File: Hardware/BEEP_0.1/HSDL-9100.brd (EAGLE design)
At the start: 21.6 x 23.6 mm, 6 parts, among them IC1 HSDL-9100

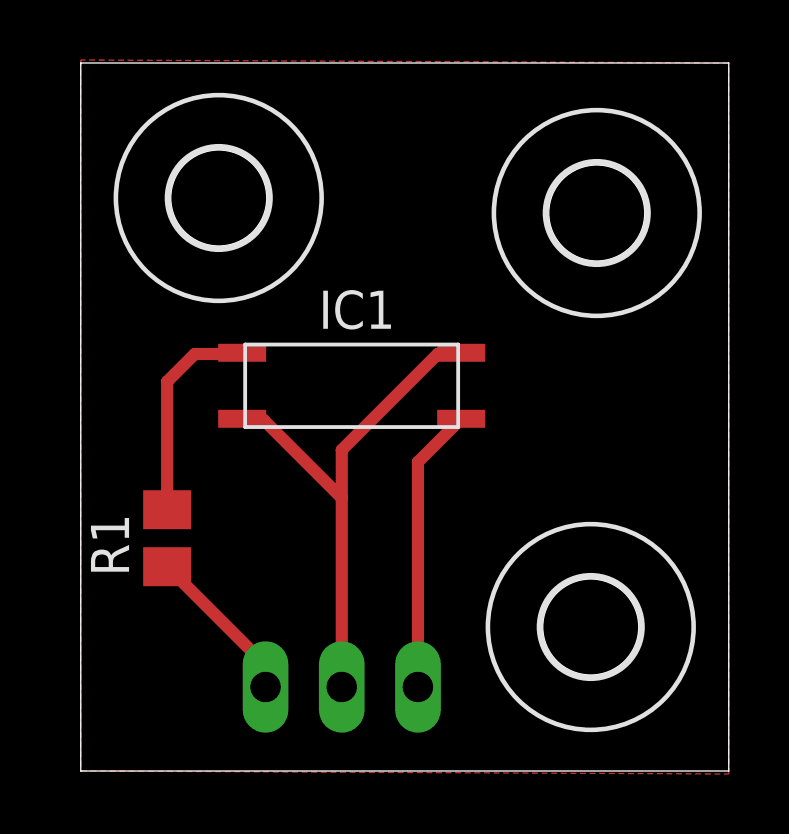
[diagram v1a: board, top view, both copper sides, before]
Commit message: Add branding ;) enhance PCBs finish Easy RGB Board add Texas Instruments libray from Element 14 add dxf import ulp for eagle add Script for easy eagle export to pdf for etching minor cleanup
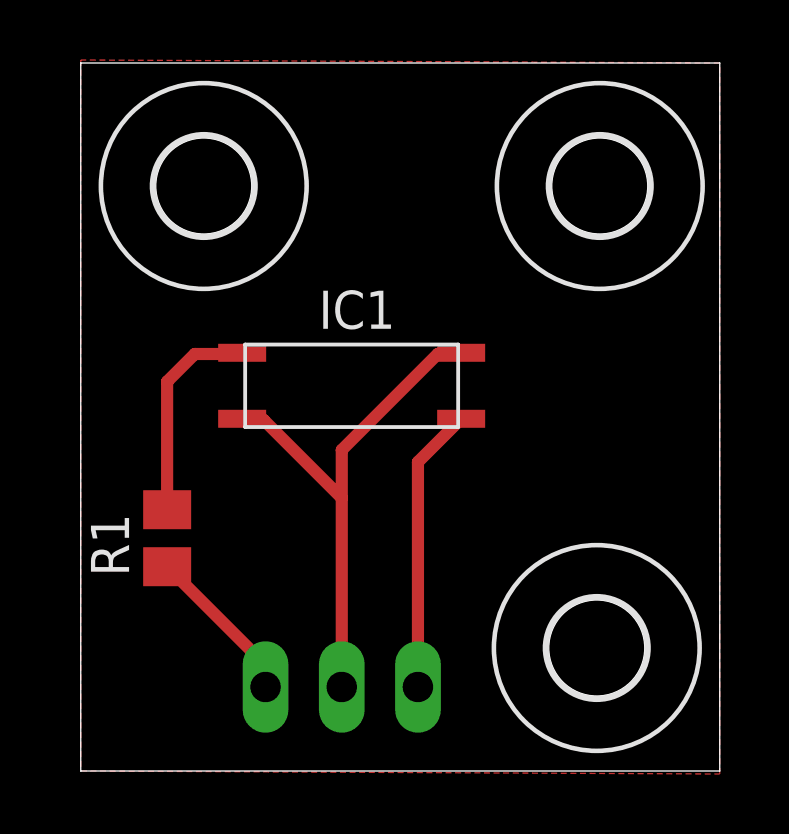
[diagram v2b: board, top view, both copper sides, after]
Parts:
- added U$1: LOGO-COPPER3, Branding:COPPER3
- moved U$4 0.91 mm to (17.3, 19.5)
- moved U$2 0.73 mm to (17.2, 4.10)
- moved U$3 0.64 mm to (4.10, 19.5)
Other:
- board size 21.6 x 23.6 mm -> 21.3 x 23.6 mm
- board text added: "HSDL-9100 v0.1.1"
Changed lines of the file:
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@@
 <layer number="43" name="vRestrict" color="2" fill="10" visible="yes" active="yes"/>
 <layer number="44" name="Drills" color="7" fill="1" visible="no" active="yes"/>
-<layer number="45" name="Holes" color="7" fill="1" visible="no" active="yes"/>
+<layer number="45" name="Holes" color="7" fill="1" visible="yes" active="yes"/>
 <layer number="46" name="Milling" color="3" fill="1" visible="no" active="yes"/>
 <layer number="47" name="Measures" color="7" fill="1" visible="no" active="yes"/>
-<layer number="48" name="Document" color="7" fill="1" visible="yes" active="yes"/>
-<layer number="49" name="Reference" color="7" fill="1" visible="yes" active="yes"/>
+<layer number="48" name="Document" color="7" fill="1" visible="no" active="yes"/>
+<layer number="49" name="Reference" color="7" fill="1" visible="no" active="yes"/>
 <layer number="51" name="tDocu" color="7" fill="1" visible="yes" active="yes"/>
 <layer number="52" name="bDocu" color="7" fill="1" visible="yes" active="yes"/>
@@
 <layer number="97" name="Info" color="7" fill="1" visible="no" active="no"/>
 <layer number="98" name="Guide" color="6" fill="1" visible="no" active="no"/>
+<layer number="100" name="tCName" color="7" fill="1" visible="yes" active="yes"/>
+<layer number="101" name="bCName" color="7" fill="1" visible="yes" active="yes"/>
 </layers>
 <board>
 <plain>
-<wire x1="0" y1="0" x2="21.6" y2="0" width="0" layer="20"/>
-<wire x1="21.6" y1="0" x2="21.6" y2="23.6" width="0" layer="20"/>
-<wire x1="21.6" y1="23.6" x2="0" y2="23.6" width="0" layer="20"/>
+<wire x1="0" y1="0" x2="21.3" y2="0" width="0" layer="20"/>
+<wire x1="21.3" y1="0" x2="21.3" y2="23.6" width="0" layer="20"/>
+<wire x1="21.3" y1="23.6" x2="0" y2="23.6" width="0" layer="20"/>
 <wire x1="0" y1="23.6" x2="0" y2="0" width="0" layer="20"/>
 <text x="7.9" y="4.6" size="1.4224" layer="26" rot="MR90">GND</text>
 <text x="5.3" y="4.7" size="1.4224" layer="26" rot="MR90">LED</text>
 <text x="10.4" y="4.6" size="1.4224" layer="26" rot="MR90">PD</text>
+<text x="15.1" y="9.4" size="0.8128" layer="100">HSDL-9100
+v0.1.1</text>
+<polygon width="0.4064" layer="41">
+<vertex x="21.3" y="15.4"/>
+<vertex x="14.9" y="15.4"/>
+<vertex x="14.9" y="7.5"/>
+<vertex x="21.3" y="7.5"/>
+</polygon>
 </plain>
 <attributes>
@@
 <attribute name="VALUE" x="4.89" y="5.975" size="1.27" layer="28" rot="MR180"/>
 </element>
-<element name="U$2" library="holes" package="3,2" value="" x="17" y="4.8"/>
-<element name="U$3" library="holes" package="3,2" value="" x="4.6" y="19.1"/>
-<element name="U$4" library="holes" package="3,2" value="" x="17.2" y="18.6"/>
+<element name="U$2" library="holes" package="3,2" value="" x="17.2" y="4.1"/>
+<element name="U$3" library="holes" package="3,2" value="" x="4.1" y="19.5"/>
+<element name="U$4" library="holes" package="3,2" value="" x="17.3" y="19.5"/>
+<element name="U$1" library="Branding" package="COPPER3" value="LOGO-COPPER3" x="15.1" y="12.6"/>
 </elements>
 <signals>
@@
 <signal name="GND">
 <polygon width="0.4064" layer="1">
-<vertex x="21.6" y="23.6"/>
+<vertex x="21.3" y="23.6"/>
 <vertex x="0" y="23.7"/>
 <vertex x="0" y="0"/>
-<vertex x="21.6" y="-0.1"/>
+<vertex x="21.3" y="-0.1"/>
 </polygon>
 <contactref element="IC1" pad="LED_K"/>
@@
 </board>
 </drawing>
+<compatibility>
+<note version="6.3" minversion="6.2.2" severity="warning">
+Since Version 6.2.2 text objects can contain more than one line,
+which will not be processed correctly with this version.
+</note>
+</compatibility>
 </eagle>

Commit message: update HSDL-9100 footprint and pcb
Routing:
- net N$4: track 9.62 -> 10.6 mm
- net GND: track 17.6 -> 17.0 mm
- net N$3: track 7.17 -> 6.65 mm
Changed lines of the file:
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@@
 <vertex x="21.3" y="7.5"/>
 </polygon>
+<wire x1="13.7" y1="11.7" x2="11.6" y2="11.7" width="0.4064" layer="41"/>
+<wire x1="11.6" y1="11.7" x2="11.6" y2="12.5" width="0.4064" layer="41"/>
+<wire x1="11.6" y1="12.5" x2="13.7" y2="12.5" width="0.4064" layer="41"/>
+<wire x1="13.7" y1="12.5" x2="13.7" y2="11.7" width="0.4064" layer="41"/>
+<wire x1="4.4" y1="13.1" x2="6.4" y2="13.1" width="0.4064" layer="41"/>
+<wire x1="6.4" y1="13.1" x2="6.4" y2="13.9" width="0.4064" layer="41"/>
+<wire x1="6.4" y1="13.9" x2="4.4" y2="13.9" width="0.4064" layer="41"/>
+<wire x1="4.4" y1="13.9" x2="4.4" y2="13.1" width="0.4064" layer="41"/>
 </plain>
 <attributes>
@@
 <contactref element="IC1" pad="LED_A"/>
 <contactref element="R1" pad="2"/>
-<wire x1="2.88" y1="8.71" x2="2.88" y2="12.98" width="0.4064" layer="1"/>
-<wire x1="2.88" y1="12.98" x2="3.8" y2="13.9" width="0.4064" layer="1"/>
-<wire x1="3.8" y1="13.9" x2="5.34" y2="13.9" width="0.4064" layer="1"/>
-<wire x1="5.34" y1="13.9" x2="5.38" y2="13.94" width="0.4064" layer="1"/>
+<wire x1="2.88" y1="8.71" x2="2.88" y2="12.48" width="0.4064" layer="1"/>
+<wire x1="2.88" y1="12.48" x2="3.8" y2="13.4" width="0.4064" layer="1"/>
+<wire x1="3.8" y1="13.4" x2="5.34" y2="13.4" width="0.4064" layer="1"/>
+<wire x1="5.34" y1="13.4" x2="5.38" y2="13.39" width="0.4064" layer="1"/>
 </signal>
 <signal name="N$4">
 <contactref element="IC1" pad="DET_A"/>
-<wire x1="12.62" y1="11.8" x2="12.68" y2="11.74" width="0.4064" layer="1"/>
-<wire x1="11.24" y1="10.3" x2="12.68" y2="11.74" width="0.4064" layer="1"/>
 <contactref element="JP1" pad="3"/>
-<wire x1="11.24" y1="2.8" x2="11.24" y2="10.3" width="0.4064" layer="1"/>
+<wire x1="11.24" y1="2.8" x2="11.24" y2="11.74" width="0.4064" layer="1"/>
+<wire x1="11.24" y1="11.74" x2="11.8" y2="12.3" width="0.4064" layer="1"/>
+<wire x1="11.8" y1="12.3" x2="12.67" y2="12.3" width="0.4064" layer="1"/>
+<wire x1="12.67" y1="12.3" x2="12.68" y2="12.29" width="0.4064" layer="1"/>
 </signal>
 <signal name="GND">
@@
 </polygon>
 <contactref element="IC1" pad="LED_K"/>
-<wire x1="6.1" y1="11.7" x2="5.42" y2="11.7" width="0.4064" layer="1"/>
-<wire x1="5.42" y1="11.7" x2="5.38" y2="11.74" width="0.4064" layer="1"/>
 <contactref element="JP1" pad="2"/>
 <contactref element="IC1" pad="DET_K"/>
-<wire x1="8.7" y1="9.1" x2="6.1" y2="11.7" width="0.4064" layer="1"/>
-<wire x1="8.7" y1="9.1" x2="8.7" y2="10.7" width="0.4064" layer="1"/>
-<wire x1="8.7" y1="10.7" x2="11.9" y2="13.9" width="0.4064" layer="1"/>
-<wire x1="11.9" y1="13.9" x2="12.64" y2="13.9" width="0.4064" layer="1"/>
-<wire x1="12.64" y1="13.9" x2="12.68" y2="13.94" width="0.4064" layer="1"/>
-<wire x1="8.7" y1="9.1" x2="8.7" y2="2.8" width="0.4064" layer="1"/>
+<wire x1="8.7" y1="10.7" x2="11.4" y2="13.4" width="0.4064" layer="1"/>
+<wire x1="8.7" y1="10.7" x2="8.7" y2="2.8" width="0.4064" layer="1"/>
+<wire x1="12.68" y1="13.39" x2="11.41" y2="13.39" width="0.4064" layer="1"/>
+<wire x1="11.41" y1="13.39" x2="11.4" y2="13.4" width="0.4064" layer="1"/>
+<wire x1="5.38" y1="12.29" x2="7.11" y2="12.29" width="0.4064" layer="1"/>
+<wire x1="7.11" y1="12.29" x2="8.7" y2="10.7" width="0.4064" layer="1"/>
 </signal>
 </signals>

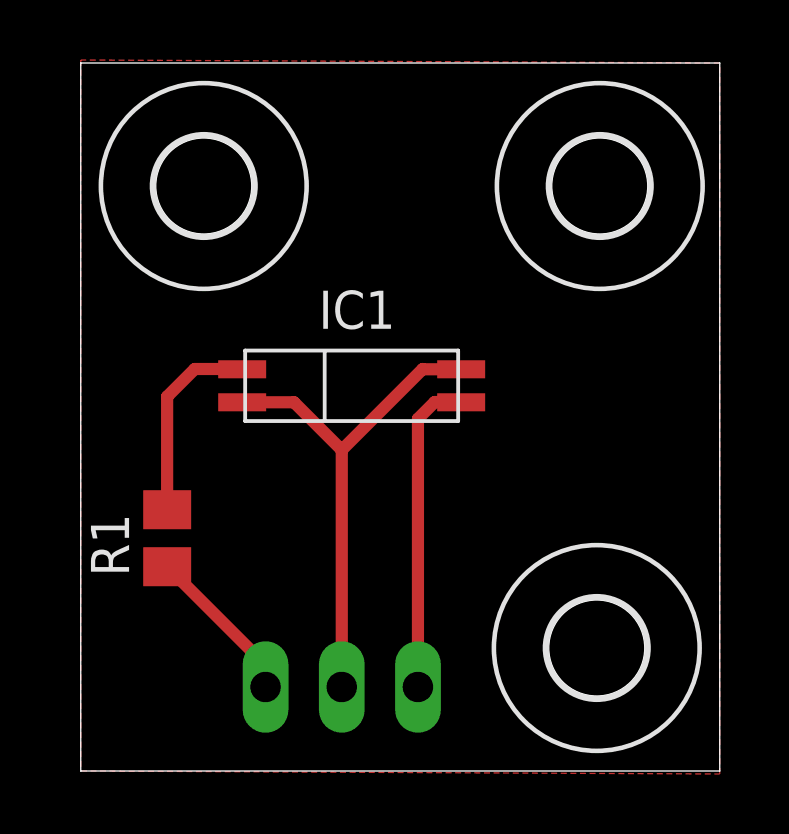
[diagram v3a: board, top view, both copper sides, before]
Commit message: enhance HSDL-9100 electronic
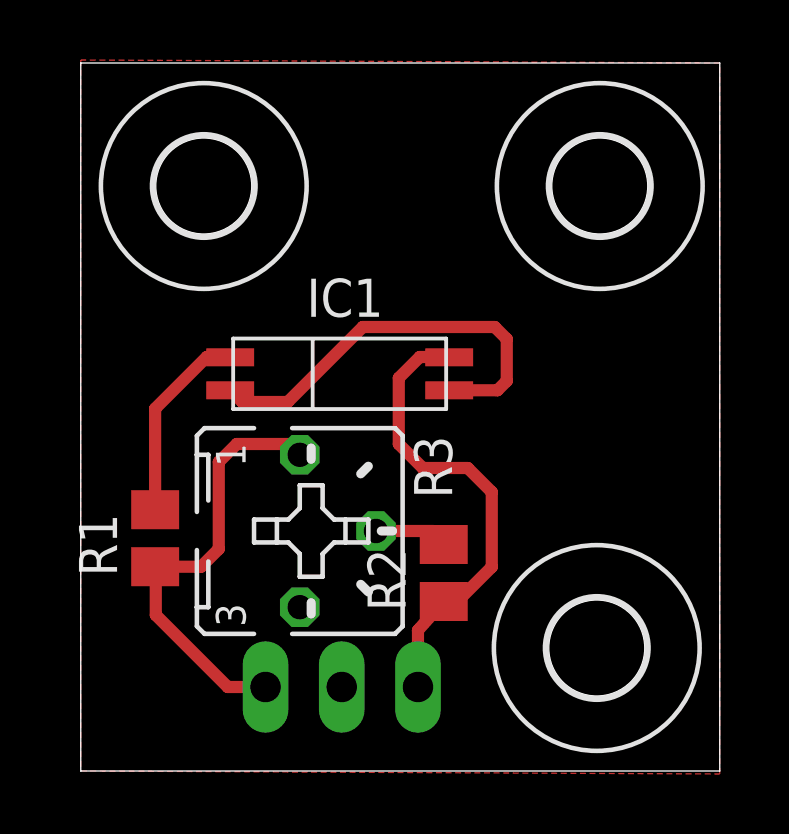
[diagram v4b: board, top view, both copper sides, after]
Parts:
- added R2: (no value), rcl:M0805
- added R3: (no value), pot:B25P
- moved IC1 0.57 mm to (8.63, 13.2)
- moved R1 0.40 mm to (2.48, 7.76)
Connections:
- removed net N$2: JP1.1, R1.1
- removed net N$4: IC1.DET_A, JP1.3
- new net ADATA: IC1.DET_K, JP1.3, R2.1
- new net N$5: R2.2, R3.S
- new net VCC: JP1.1, R1.1, R3.A
- net GND: now also IC1.DET_A; no longer IC1.DET_K
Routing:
- net ADATA: track 0.00 -> 15.8 mm
- net VCC: track 0.00 -> 14.9 mm
- net N$4: track 10.6 -> 0.00 mm
- net N$2: track 5.37 -> 0.00 mm
- net GND: track 17.0 -> 14.0 mm
- net N$5: track 0.00 -> 2.48 mm
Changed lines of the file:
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@@
 <vertex x="21.3" y="7.5"/>
 </polygon>
-<wire x1="13.7" y1="11.7" x2="11.6" y2="11.7" width="0.4064" layer="41"/>
-<wire x1="11.6" y1="11.7" x2="11.6" y2="12.5" width="0.4064" layer="41"/>
-<wire x1="11.6" y1="12.5" x2="13.7" y2="12.5" width="0.4064" layer="41"/>
-<wire x1="13.7" y1="12.5" x2="13.7" y2="11.7" width="0.4064" layer="41"/>
-<wire x1="4.4" y1="13.1" x2="6.4" y2="13.1" width="0.4064" layer="41"/>
-<wire x1="6.4" y1="13.1" x2="6.4" y2="13.9" width="0.4064" layer="41"/>
-<wire x1="6.4" y1="13.9" x2="4.4" y2="13.9" width="0.4064" layer="41"/>
-<wire x1="4.4" y1="13.9" x2="4.4" y2="13.1" width="0.4064" layer="41"/>
+<wire x1="4.3" y1="14.4" x2="6" y2="14.4" width="0.4064" layer="41"/>
+<wire x1="6" y1="14.4" x2="6" y2="13.4" width="0.4064" layer="41"/>
+<wire x1="6" y1="13.4" x2="6.4" y2="13.4" width="0.4064" layer="41"/>
+<wire x1="6.4" y1="13.4" x2="6.4" y2="14.4" width="0.4064" layer="41"/>
+<wire x1="13.3" y1="14.3" x2="10.8" y2="14.3" width="0.4064" layer="41"/>
+<wire x1="10.8" y1="14.3" x2="10.8" y2="13.7" width="0.4064" layer="41"/>
+<wire x1="13.3" y1="14.3" x2="13.3" y2="13.4" width="0.4064" layer="41"/>
 </plain>
 <attributes>
@@
 </autorouter>
 <elements>
-<element name="IC1" library="BEEP" package="HSDL-9100" value="HSDL-9100" x="9.03" y="12.84" smashed="yes">
-<attribute name="NAME" x="7.93" y="14.74" size="1.27" layer="25"/>
-<attribute name="VALUE" x="4.23" y="9.74" size="1.27" layer="27"/>
+<element name="IC1" library="BEEP" package="HSDL-9100" value="HSDL-9100" x="8.63" y="13.24" smashed="yes">
+<attribute name="NAME" x="7.53" y="15.14" size="1.27" layer="25"/>
+<attribute name="VALUE" x="3.83" y="10.14" size="1.27" layer="27"/>
 </element>
-<element name="R1" library="rcl" package="M0805" value="" x="2.88" y="7.76" rot="R90"/>
+<element name="R1" library="rcl" package="M0805" value="" x="2.48" y="7.76" rot="R90"/>
 <element name="JP1" library="pinhead" package="1X03" value="" x="8.7" y="2.8" smashed="yes" rot="MR180">
 <attribute name="VALUE" x="4.89" y="5.975" size="1.27" layer="28" rot="MR180"/>
@@
 <element name="U$4" library="holes" package="3,2" value="" x="17.3" y="19.5"/>
 <element name="U$1" library="Branding" package="COPPER3" value="LOGO-COPPER3" x="15.1" y="12.6"/>
+<element name="R2" library="rcl" package="M0805" value="" x="12.1" y="6.6" rot="R90"/>
+<element name="R3" library="pot" package="B25P" value="" x="7.3" y="8" rot="R270"/>
 </elements>
 <signals>
-<signal name="N$2">
-<contactref element="R1" pad="1"/>
-<wire x1="6.16" y1="3.53" x2="2.88" y2="6.81" width="0.4064" layer="1"/>
-<contactref element="JP1" pad="1"/>
-<wire x1="6.16" y1="3.53" x2="6.16" y2="2.8" width="0.4064" layer="1"/>
-</signal>
 <signal name="N$3">
 <contactref element="IC1" pad="LED_A"/>
 <contactref element="R1" pad="2"/>
-<wire x1="2.88" y1="8.71" x2="2.88" y2="12.48" width="0.4064" layer="1"/>
-<wire x1="2.88" y1="12.48" x2="3.8" y2="13.4" width="0.4064" layer="1"/>
-<wire x1="3.8" y1="13.4" x2="5.34" y2="13.4" width="0.4064" layer="1"/>
-<wire x1="5.34" y1="13.4" x2="5.38" y2="13.39" width="0.4064" layer="1"/>
-</signal>
-<signal name="N$4">
-<contactref element="IC1" pad="DET_A"/>
-<contactref element="JP1" pad="3"/>
-<wire x1="11.24" y1="2.8" x2="11.24" y2="11.74" width="0.4064" layer="1"/>
-<wire x1="11.24" y1="11.74" x2="11.8" y2="12.3" width="0.4064" layer="1"/>
-<wire x1="11.8" y1="12.3" x2="12.67" y2="12.3" width="0.4064" layer="1"/>
-<wire x1="12.67" y1="12.3" x2="12.68" y2="12.29" width="0.4064" layer="1"/>
+<wire x1="2.48" y1="8.71" x2="2.48" y2="12.08" width="0.4064" layer="1"/>
+<wire x1="2.48" y1="12.08" x2="4.2" y2="13.8" width="0.4064" layer="1"/>
+<wire x1="4.2" y1="13.8" x2="4.94" y2="13.8" width="0.4064" layer="1"/>
+<wire x1="4.94" y1="13.8" x2="4.98" y2="13.79" width="0.4064" layer="1"/>
 </signal>
 <signal name="GND">
@@
 </polygon>
 <contactref element="IC1" pad="LED_K"/>
+<contactref element="IC1" pad="DET_A"/>
+<wire x1="12.28" y1="12.69" x2="13.89" y2="12.69" width="0.4064" layer="1"/>
+<wire x1="13.89" y1="12.69" x2="14.2" y2="13" width="0.4064" layer="1"/>
+<wire x1="14.2" y1="13" x2="14.2" y2="14.4" width="0.4064" layer="1"/>
+<wire x1="14.2" y1="14.4" x2="13.8" y2="14.8" width="0.4064" layer="1"/>
+<wire x1="13.8" y1="14.8" x2="9.4" y2="14.8" width="0.4064" layer="1"/>
+<wire x1="9.4" y1="14.8" x2="6.9" y2="12.3" width="0.4064" layer="1"/>
+<wire x1="6.9" y1="12.3" x2="5.39" y2="12.3" width="0.4064" layer="1"/>
+<wire x1="5.39" y1="12.3" x2="4.98" y2="12.69" width="0.4064" layer="1"/>
 <contactref element="JP1" pad="2"/>
+</signal>
+<signal name="ADATA">
 <contactref element="IC1" pad="DET_K"/>
-<wire x1="8.7" y1="10.7" x2="11.4" y2="13.4" width="0.4064" layer="1"/>
-<wire x1="8.7" y1="10.7" x2="8.7" y2="2.8" width="0.4064" layer="1"/>
-<wire x1="12.68" y1="13.39" x2="11.41" y2="13.39" width="0.4064" layer="1"/>
-<wire x1="11.41" y1="13.39" x2="11.4" y2="13.4" width="0.4064" layer="1"/>
-<wire x1="5.38" y1="12.29" x2="7.11" y2="12.29" width="0.4064" layer="1"/>
-<wire x1="7.11" y1="12.29" x2="8.7" y2="10.7" width="0.4064" layer="1"/>
+<contactref element="R2" pad="1"/>
+<wire x1="12.05" y1="5.5" x2="12.1" y2="5.65" width="0.4064" layer="1"/>
+<wire x1="12.1" y1="5.65" x2="12.55" y2="5.65" width="0.4064" layer="1"/>
+<wire x1="12.55" y1="5.65" x2="13.7" y2="6.8" width="0.4064" layer="1"/>
+<wire x1="13.7" y1="6.8" x2="13.7" y2="9.3" width="0.4064" layer="1"/>
+<wire x1="13.7" y1="9.3" x2="12.9" y2="10.1" width="0.4064" layer="1"/>
+<wire x1="12.9" y1="10.1" x2="11.4" y2="10.1" width="0.4064" layer="1"/>
+<wire x1="11.4" y1="10.1" x2="10.6" y2="10.9" width="0.4064" layer="1"/>
+<wire x1="10.6" y1="10.9" x2="10.6" y2="13.1" width="0.4064" layer="1"/>
+<wire x1="10.6" y1="13.1" x2="11.3" y2="13.8" width="0.4064" layer="1"/>
+<wire x1="11.3" y1="13.8" x2="12.17" y2="13.8" width="0.4064" layer="1"/>
+<wire x1="12.17" y1="13.8" x2="12.28" y2="13.79" width="0.4064" layer="1"/>
+<contactref element="JP1" pad="3"/>
+<wire x1="11.24" y1="2.8" x2="11.24" y2="4.69" width="0.4064" layer="1"/>
+<wire x1="11.24" y1="4.69" x2="12.1" y2="5.65" width="0.4064" layer="1"/>
+</signal>
+<signal name="N$5">
+<contactref element="R2" pad="2"/>
+<contactref element="R3" pad="S"/>
+<wire x1="9.84" y1="8" x2="11.75" y2="8" width="0.4064" layer="1"/>
+<wire x1="11.75" y1="8" x2="12.1" y2="7.55" width="0.4064" layer="1"/>
+</signal>
+<signal name="VCC">
+<contactref element="R3" pad="A"/>
+<contactref element="R1" pad="1"/>
+<contactref element="JP1" pad="1"/>
+<wire x1="6.16" y1="2.8" x2="4.9" y2="2.8" width="0.4064" layer="1"/>
+<wire x1="4.9" y1="2.8" x2="2.5" y2="5.2" width="0.4064" layer="1"/>
+<wire x1="2.5" y1="5.2" x2="2.5" y2="6.49" width="0.4064" layer="1"/>
+<wire x1="2.5" y1="6.49" x2="2.48" y2="6.81" width="0.4064" layer="1"/>
+<wire x1="2.48" y1="6.81" x2="4.01" y2="6.81" width="0.4064" layer="1"/>
+<wire x1="4.01" y1="6.81" x2="4.6" y2="7.4" width="0.4064" layer="1"/>
+<wire x1="4.6" y1="7.4" x2="4.6" y2="10.3" width="0.4064" layer="1"/>
+<wire x1="4.6" y1="10.3" x2="5.2" y2="10.9" width="0.4064" layer="1"/>
+<wire x1="5.2" y1="10.9" x2="7.34" y2="10.9" width="0.4064" layer="1"/>
+<wire x1="7.34" y1="10.9" x2="7.3" y2="10.54" width="0.4064" layer="1"/>
 </signal>
 </signals>
